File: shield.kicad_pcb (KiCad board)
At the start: 4 copper layers, 160 x 130 mm, 179 parts, among them J1 NAPPE_ADC1, J10 OLED_SPI_2x8, J13 NAPPE_LOGIC, J14 NAPPE_COM, J15 USBC-PD, J16 CONN_2PIN, J17 DEVKIT_C2000_A, J18 DEVKIT_C2000_B, J2 NAPPE_ADC2, J3 NAPPE_PWM, J4 NAPPE_GPIO1, J7 ESP32_C6_DEVKITC_1_J1, J8 ESP32_C6_DEVKITC_1_J3, J9 J_PWR_11-25V, Q1 SQJ459EP-T2_GE3, U1 LDO_3V3_ISO, U2 NCM3S1205MC, U3 NCM3S1205MC, U4 ER-OLEDM032-1, U5 STUSB4531QTR

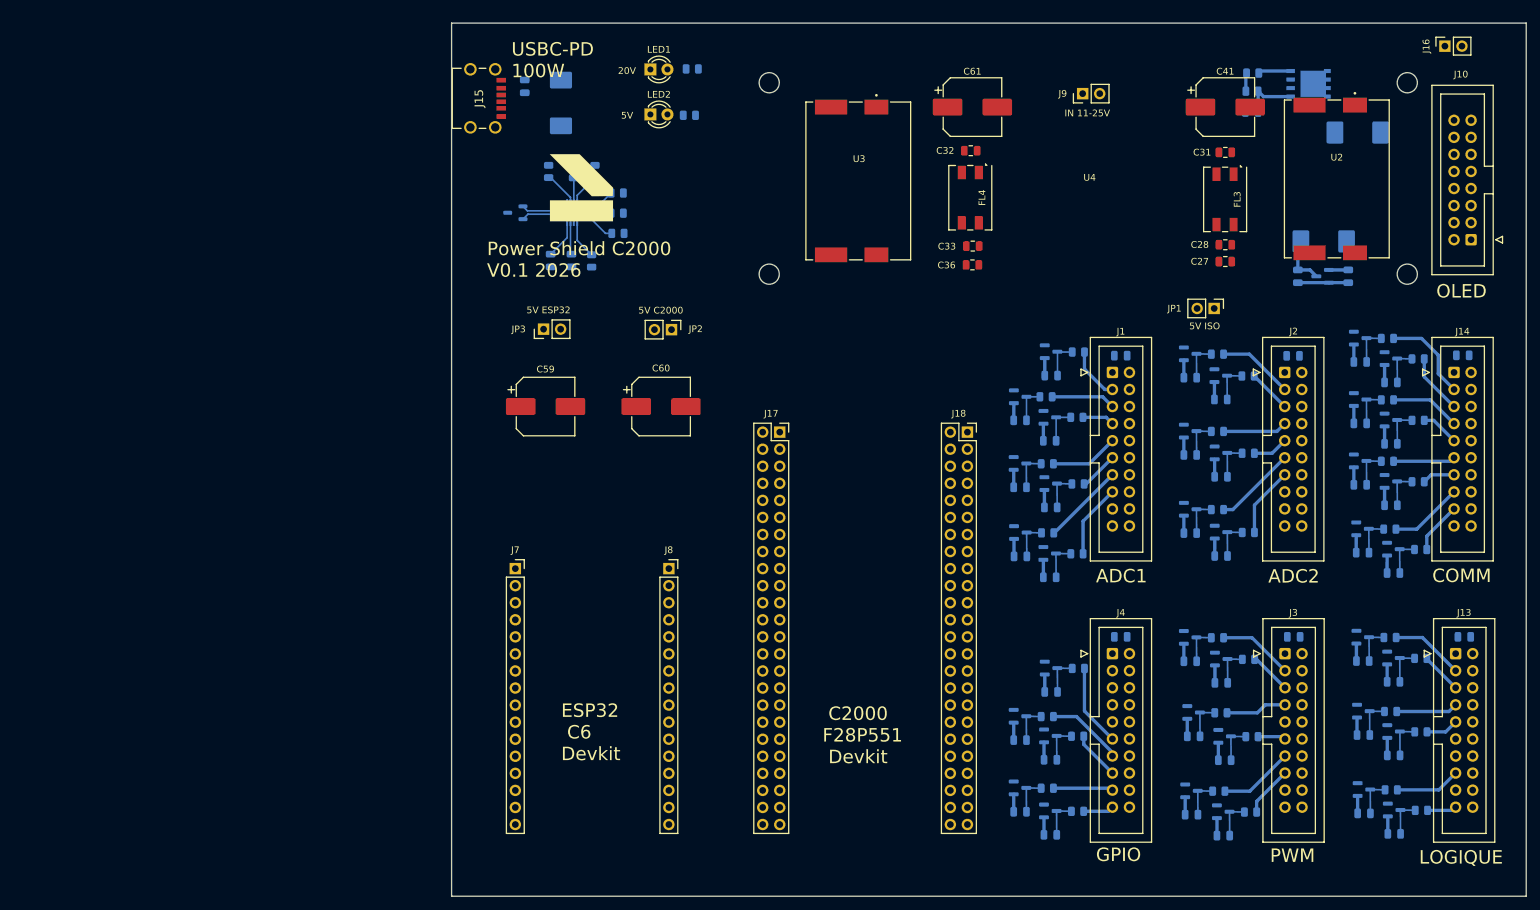
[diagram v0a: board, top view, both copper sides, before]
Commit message: Remplace DPC817 (NRND, empreinte maison) par TCMT1100 (Vishay, standard)
U7 passe d'un optocoupleur Diodes Inc. en boitier SL-4 fait main a un
TCMT1100 Vishay dont le symbole ET l'empreinte (SOP-4_4.4x2.6mm_P1.27mm)
sont stock KiCad - brochage identique, aucun rewiring necessaire.
Footprint PCB reconstruit a la main via kipy (pads, silkscreen,
courtyard, contour fab, identite de librairie). Route et groupe aussi
les 5 nouveaux trios de protection ADC (D44-48/R50-54/C66-70) en
copiant le gabarit des trios existants, et uniformise a 0,5mm toutes
les pistes internes des 43 groupes PROT_*.

Decision #28 dans doc/decisions.md.

Co-Authored-By: Claude Sonnet 5 <noreply@anthropic.com>
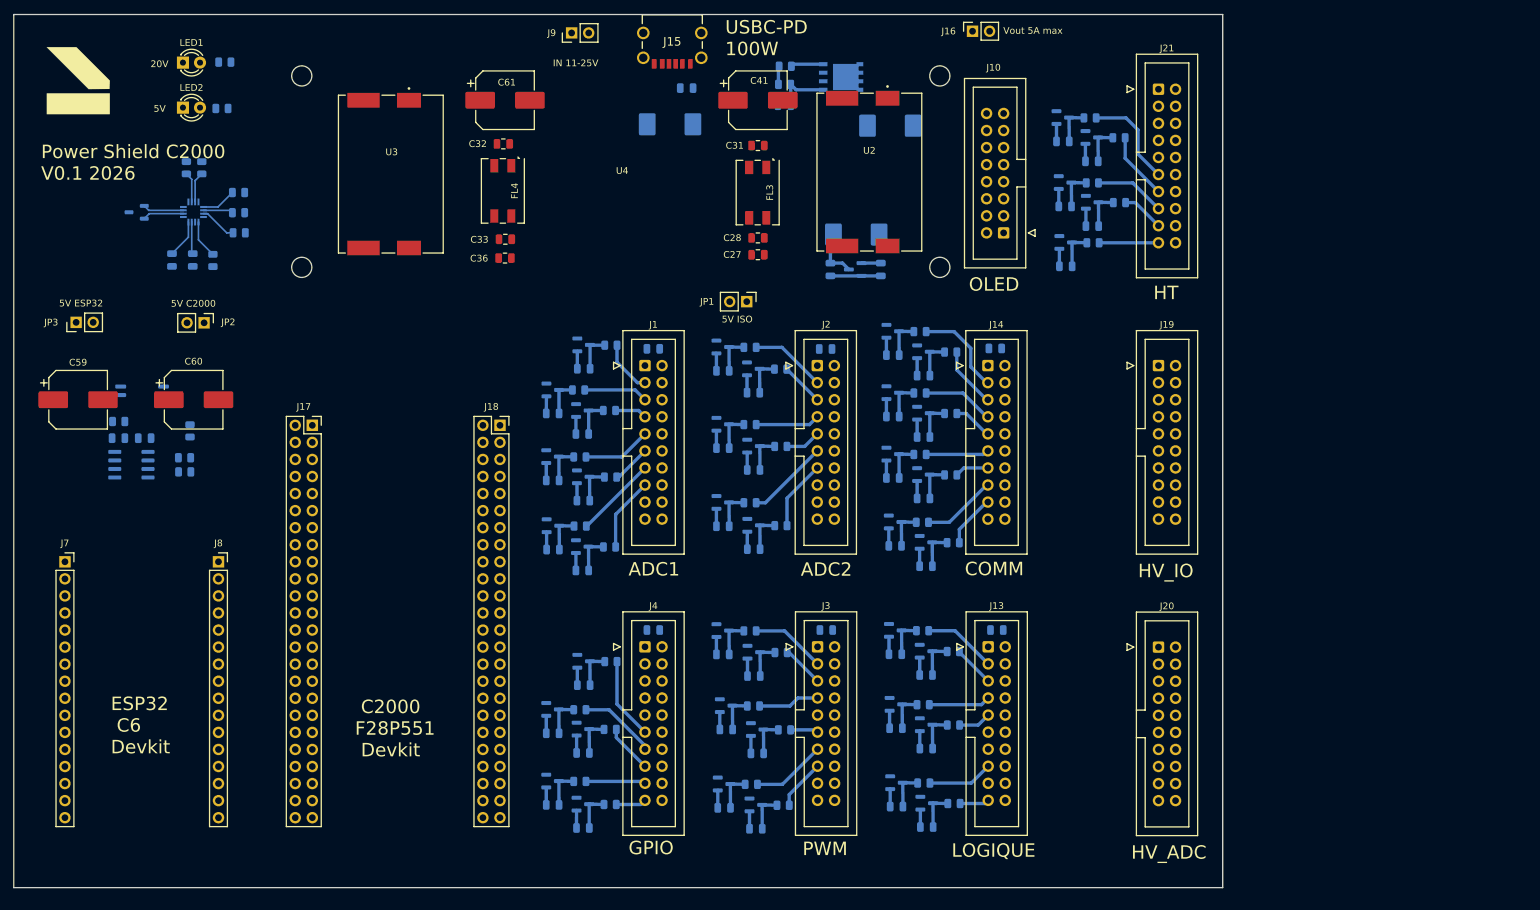
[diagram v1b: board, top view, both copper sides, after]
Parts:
- added C66: 100pF, Capacitor_SMD:C_0805_2012Metric, B.Cu at (192.0, 45.6)
- added C67: 100pF, Capacitor_SMD:C_0805_2012Metric, B.Cu at (196.3, 48.6)
- added C68: 100pF, Capacitor_SMD:C_0805_2012Metric, B.Cu at (192.4, 55.3)
- added C69: 100pF, Capacitor_SMD:C_0805_2012Metric, B.Cu at (196.4, 58.2)
- added C70: 100pF, Capacitor_SMD:C_0805_2012Metric, B.Cu at (192.4, 64.2)
- added C71: 100nF, Capacitor_SMD:C_0805_2012Metric, B.Cu at (55.3, 89.8)
- added C72: 100nF, Capacitor_SMD:C_0805_2012Metric, B.Cu at (51.4, 89.8)
- added D44: BAT54S, Package_TO_SOT_SMD:SOT-23, B.Cu at (192.0, 42.1)
- added D45: BAT54S, Package_TO_SOT_SMD:SOT-23, B.Cu at (196.3, 45.0)
- added D46: BAT54S, Package_TO_SOT_SMD:SOT-23, B.Cu at (192.3, 51.7)
- added D47: BAT54S, Package_TO_SOT_SMD:SOT-23, B.Cu at (196.4, 54.7)
- added D48: BAT54S, Package_TO_SOT_SMD:SOT-23, B.Cu at (192.4, 60.7)
- added J19: NAPPE_HV_ADC, Connector_IDC:IDC-Header_2x10_P2.54mm_Vertical, F.Cu at (206.2, 79.0)
- added J20: NAPPE_HV_DIO, Connector_IDC:IDC-Header_2x10_P2.54mm_Vertical, F.Cu at (206.2, 120.9)
- added J21: NAPPE_FILAMENT_HT, Connector_IDC:IDC-Header_2x10_P2.54mm_Vertical, F.Cu at (206.2, 37.8)
- added R50: 100R, Resistor_SMD:R_0805_2012Metric, B.Cu at (196.1, 42.1)
- added R51: 100R, Resistor_SMD:R_0805_2012Metric, B.Cu at (200.4, 45.1)
- added R52: 100R, Resistor_SMD:R_0805_2012Metric, B.Cu at (196.4, 51.8)
- added R53: 22R, Resistor_SMD:R_0805_2012Metric, B.Cu at (200.4, 54.7)
- added R54: 100R, Resistor_SMD:R_0805_2012Metric, B.Cu at (196.5, 60.7)
- added R55: 2.2k, Resistor_SMD:R_0805_2012Metric, B.Cu at (61.5, 49.5)
- added R56: 2.2k, Resistor_SMD:R_0805_2012Metric, B.Cu at (63.8, 49.5)
- added R57: 330R, Resistor_SMD:R_0805_2012Metric, B.Cu at (51.4, 87.3)
- added U6: ISO1640BD, Package_SO:SOIC-8_3.9x4.9mm_P1.27mm, B.Cu at (53.3, 93.8)
- added U7: TCMT1100, Package_SO:SOP-4_4.4x2.6mm_P1.27mm, B.Cu at (54.9, 82.7)
- moved J9 76.6 mm to (118.9, 29.5)
- moved Lebel Audio 76.6 mm to (45.7, 36.6)
- moved R46 71.9 mm to (61.2, 92.7), turned to 0 degrees
- moved R47 71.6 mm to (62.0, 88.7), turned to -90 degrees
- moved J16 70.4 mm to (178.6, 29.2)
- moved R45 70.3 mm to (61.3, 94.8), turned to 0 degrees
- moved C21 69.6 mm to (120.6, 136.7)
- moved C32 69.6 mm to (108.7, 46.0)
- moved C36 69.6 mm to (109.0, 63.0)
- moved C61 69.6 mm to (109.0, 39.5)
- moved C7 69.6 mm to (120.5, 109.5)
- moved D2 69.6 mm to (116.1, 82.6)
- moved D7 69.6 mm to (116.1, 102.8)
- moved J17 69.6 mm to (80.3, 87.9)
- moved J18 69.6 mm to (108.2, 87.9)
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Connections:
- C62 pad 2: GND -> GND_PRI
- C63 pad 2: GND -> GND_PRI
- C64 pad 2: GND -> GND_PRI
- C65 pad 2: GND -> GND_PRI
- D40 pad 2: GND -> GND_PRI
- D41 pad 2: GND -> GND_PRI
- D43 pad 3: GND -> GND_PRI
- J15 pad A12: GND -> GND_PRI
- J15 pad B12: GND -> GND_PRI
- J15 pad MH1: GND -> GND_PRI
- J15 pad MH2: GND -> GND_PRI
- J15 pad MH3: GND -> GND_PRI
- J15 pad MH4: GND -> GND_PRI
- J16 pad 2: GND -> GND_PRI
- J17 pad 16: ADC_8 -> ADC_8_MCU
- J17 pad 17: ADC_9 -> ADC_9_MCU
- J17 pad 20: ADC_10 -> ADC_10_MCU
- J17 pad 21: ADC_11 -> ADC_11_MCU
- J17 pad 24: ADC_12 -> ADC_12_MCU
- J8 pad 5: STUSB_SDA -> ESP32_SDA_ISO
- J8 pad 6: STUSB_SCL -> ESP32_SCL_ISO
- J8 pad 7: STUSB_ALERT -> ESP32_ALERT_ISO
- R39 pad 2: GND -> GND_PRI
- R45 pad 1: STUSB_SCL -> ESP32_SCL_ISO
- R46 pad 1: STUSB_SDA -> ESP32_SDA_ISO
- R47 pad 1: STUSB_ALERT -> ESP32_ALERT_ISO
- U5 pad 12: GND -> GND_PRI
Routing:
- net Vht: track 0.00 -> 14.9 mm
- net GND: track 106.2 -> 119.2 mm
- net I_Shunt_ht: track 0.00 -> 10.5 mm
- net Temp_ht: track 0.00 -> 10.1 mm
- net V_bias: track 0.00 -> 8.84 mm
- net I_Shunt_ht_comp: track 0.00 -> 6.32 mm
- net ADC_12_MCU: track 0.00 -> 5.76 mm
- net ADC_10_MCU: track 0.00 -> 5.76 mm
- net ADC_11_MCU: track 0.00 -> 5.76 mm
- net ADC_9_MCU: track 0.00 -> 5.76 mm
- net ADC_8_MCU: track 0.00 -> 5.76 mm
- net STUSB_ALERT: track 4.80 -> 0.00 mm
- net STUSB_SDA: track 3.68 -> 4.59 mm
- net STUSB_SCL: track 5.22 -> 4.51 mm
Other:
- board size 160 x 130 mm -> 180 x 130 mm
- board text added: "HT"
- board text added: "HV_ADC"
- board text added: "HV_IO"
- board text added: "Vout 5A max"
